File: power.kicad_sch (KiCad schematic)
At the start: 40 parts, among them J201 ATX-24, SW201 NM, U201 OPA2197xD, U202 AMS1117-3.3

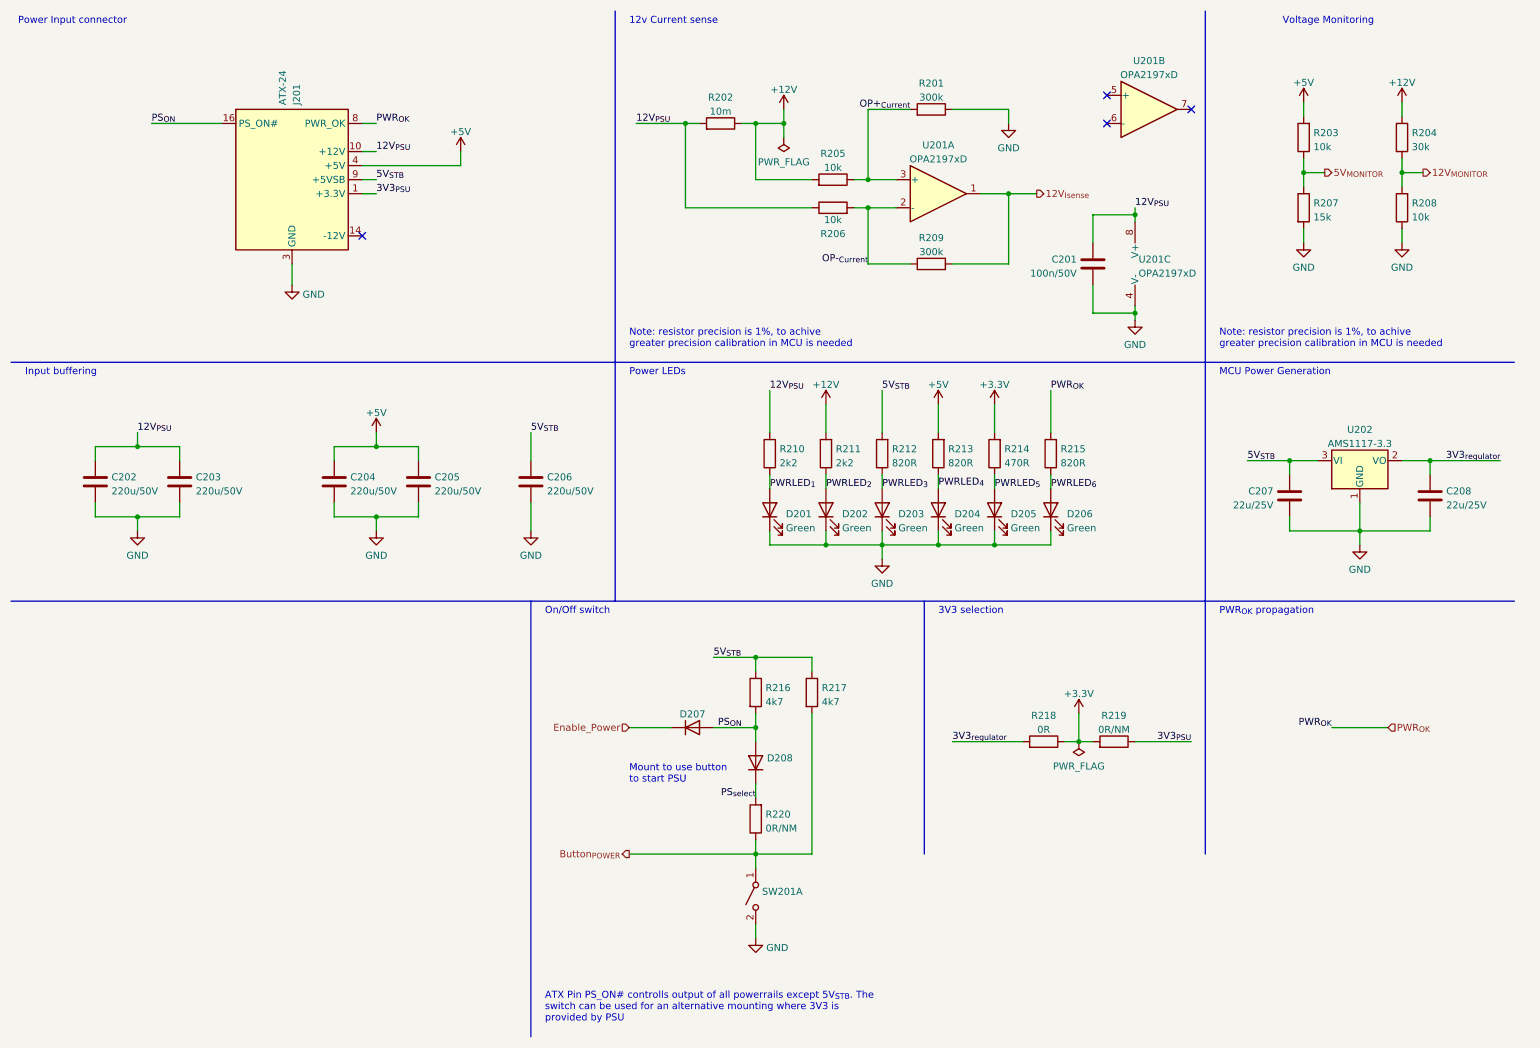
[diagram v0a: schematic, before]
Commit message: Added Testpoints
Schematic and PCB updated
Also probably some other smaller changes that I forgot about
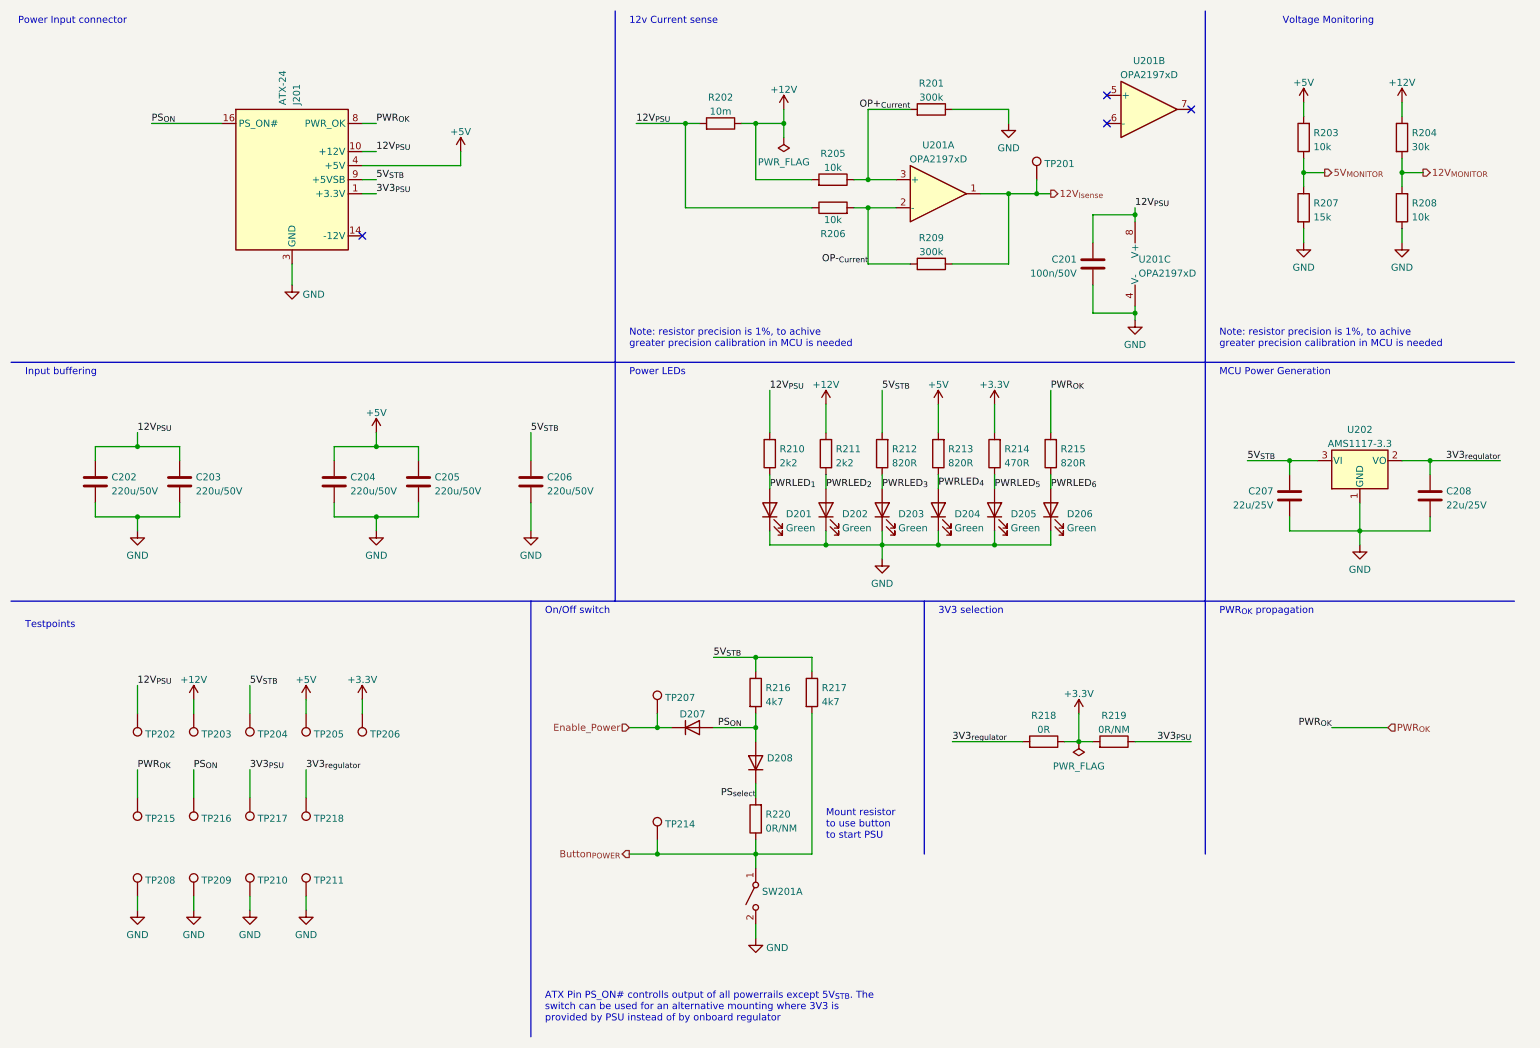
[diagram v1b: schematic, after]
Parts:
- added TP201, TP202, TP203, TP204, TP205, TP206, TP207, TP208, TP209, TP210, TP211, TP214, TP215, TP216, TP217, TP218: TestPoint, TestPoint:TestPoint_Loop_D1.80mm_Drill1.0mm_Beaded, symbol Connector:TestPoint
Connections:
- net +12V: now also TP203.1
- net +3.3V: now also TP206.1
- net +5V: now also TP205.1
- net 12V_{Isense}: now also TP201.1
- net 12V_{PSU}: now also TP202.1
- net 3V3_{PSU}: now also TP217.1
- net 3V3_{regulator}: now also TP218.1
- net 5V_{STB}: now also TP204.1
- net Button_{POWER}: now also TP214.1
- net Enable_Power: now also TP207.1
- net GND: now also TP208.1, TP209.1, TP210.1, TP211.1
- net PS_{ON}: now also TP216.1
- net PWR_{OK}: now also TP215.1
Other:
- note added: "ATX Pin PS_ON# controlls output of all powerrails except 5V_{STB}. The switch can be used for an alternative mounting where 3V3 is provided by PSU instead of by onboard regulator"
- note added: "Mount resistor to use button to start PSU"
- note added: "Testpoints"
- note removed: "ATX Pin PS_ON# controlls output of all powerrails except 5V_{STB}. The switch can be used for an alternative mounting where 3V3 is provided by PSU"
- note removed: "Mount to use button to start PSU"

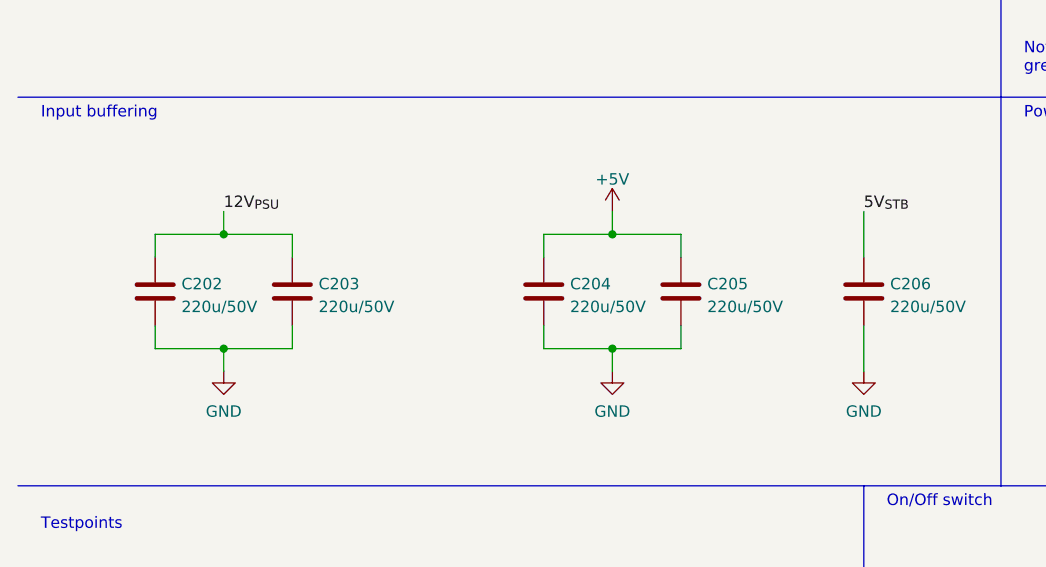
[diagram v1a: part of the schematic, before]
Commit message: Fix DRCs and BOM errors
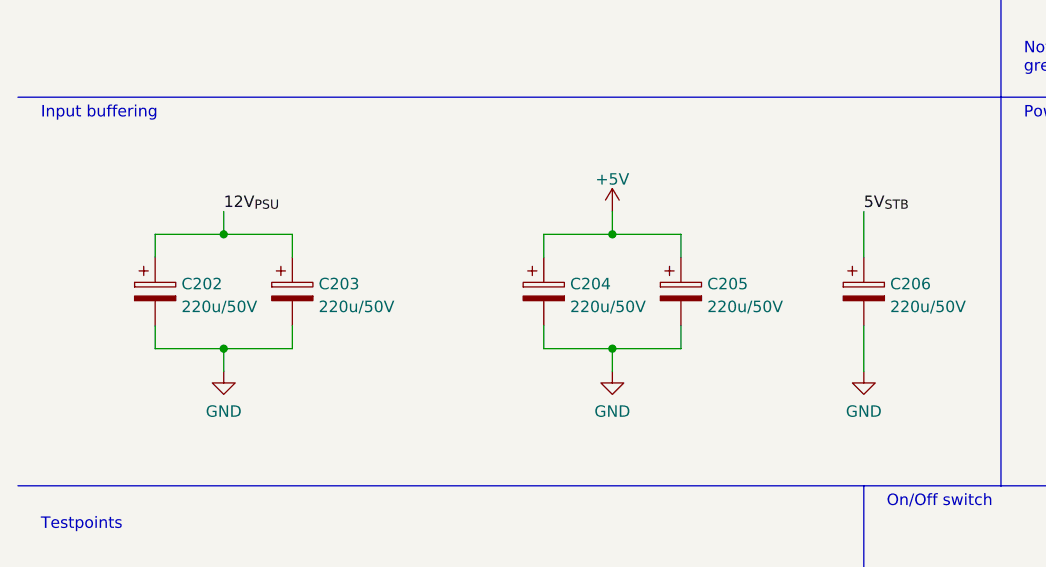
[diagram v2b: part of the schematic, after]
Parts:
- C202, C203, C204, C205, C206: symbol Device:C -> Device:C_Polarized
- J201: LCSC (none) -> C500834
- SW201: value NM -> SW_MEC_5G; LCSC (none) -> C318884
- U201: LCSC (none) -> C139363
- U202: LCSC (none) -> C6186
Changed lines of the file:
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@@
+      (effects (font (size 1.27 1.27)) hide)
+    )
+    (property "LCSC" "C139363" (id 4) (at 180.34 45.72 0)
       (effects (font (size 1.27 1.27)) hide)
     )
@@
       (effects (font (size 1.27 1.27)) hide)
     )
+    (property "LCSC" "C6186" (id 4) (at 256.54 93.98 0)
+      (effects (font (size 1.27 1.27)) hide)
+    )
     (pin "1")
     (pin "2")
@@
     (pin "1")
   )
-  (symbol (lib_id "Device:C") (at 27.94 97.79 0) (unit 1)
+  (symbol (lib_id "Device:C_Polarized") (at 27.94 97.79 0) (unit 1)
     (in_bom yes) (on_board yes) (fields_autoplaced)
     (property "Reference" "C202" (id 0) (at 30.861 96.9553 0)
@@
     (pin "2")
   )
-  (symbol (lib_id "Device:C") (at 86.36 97.79 0) (unit 1)
+  (symbol (lib_id "Device:C_Polarized") (at 86.36 97.79 0) (unit 1)
     (in_bom yes) (on_board yes) (fields_autoplaced)
     (property "Reference" "C205" (id 0) (at 89.281 96.9553 0)
@@
     (pin "1")
   )
-  (symbol (lib_id "Device:C") (at 71.12 97.79 0) (unit 1)
+  (symbol (lib_id "Device:C_Polarized") (at 71.12 97.79 0) (unit 1)
     (in_bom yes) (on_board yes) (fields_autoplaced)
     (property "Reference" "C204" (id 0) (at 74.041 96.9553 0)
@@
     )
     (property "Datasheet" "https://www.intel.com/content/dam/www/public/us/en/documents/guides/power-supply-design-guide-june.pdf#page=33" (id 3) (at 124.46 57.15 0)
+      (effects (font (size 1.27 1.27)) hide)
+    )
+    (property "LCSC" "C500834" (id 4) (at 63.5 43.18 0)
       (effects (font (size 1.27 1.27)) hide)
     )
@@
       (effects (font (size 1.27 1.27)) hide)
     )
+    (property "LCSC" "C139363" (id 4) (at 215.9 58.42 0)
+      (effects (font (size 1.27 1.27)) hide)
+    )
     (pin "1")
     (pin "2")
@@
       (effects (font (size 1.27 1.27)) hide)
     )
+    (property "LCSC" "C139363" (id 4) (at 218.44 30.48 0)
+      (effects (font (size 1.27 1.27)) hide)
+    )
     (pin "1")
     (pin "2")
@@
     (pin "1")
   )
-  (symbol (lib_id "Device:C") (at 43.18 97.79 0) (unit 1)
+  (symbol (lib_id "Device:C_Polarized") (at 43.18 97.79 0) (unit 1)
     (in_bom yes) (on_board yes) (fields_autoplaced)
     (property "Reference" "C203" (id 0) (at 46.101 96.9553 0)
@@
     (pin "2")
   )
-  (symbol (lib_id "Device:C") (at 106.68 97.79 0) (unit 1)
+  (symbol (lib_id "Device:C_Polarized") (at 106.68 97.79 0) (unit 1)
     (in_bom yes) (on_board yes) (fields_autoplaced)
     (property "Reference" "C206" (id 0) (at 109.601 96.9553 0)
@@
       (effects (font (size 1.27 1.27)) (justify right))
     )
-    (property "Value" "NM" (id 1) (at 148.463 174.4222 90)
+    (property "Value" "SW_MEC_5G" (id 1) (at 148.463 174.4222 90)
       (effects (font (size 1.27 1.27)) (justify right) hide)
     )
@@
       (effects (font (size 1.27 1.27)) hide)
     )
+    (property "LCSC" "C318884" (id 4) (at 147.32 172.72 0)
+      (effects (font (size 1.27 1.27)) hide)
+    )
